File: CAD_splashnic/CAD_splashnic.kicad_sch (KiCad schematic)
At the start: 3 parts, among them J1 Screw_Terminal_01x03, U1 STM32G431KBTx

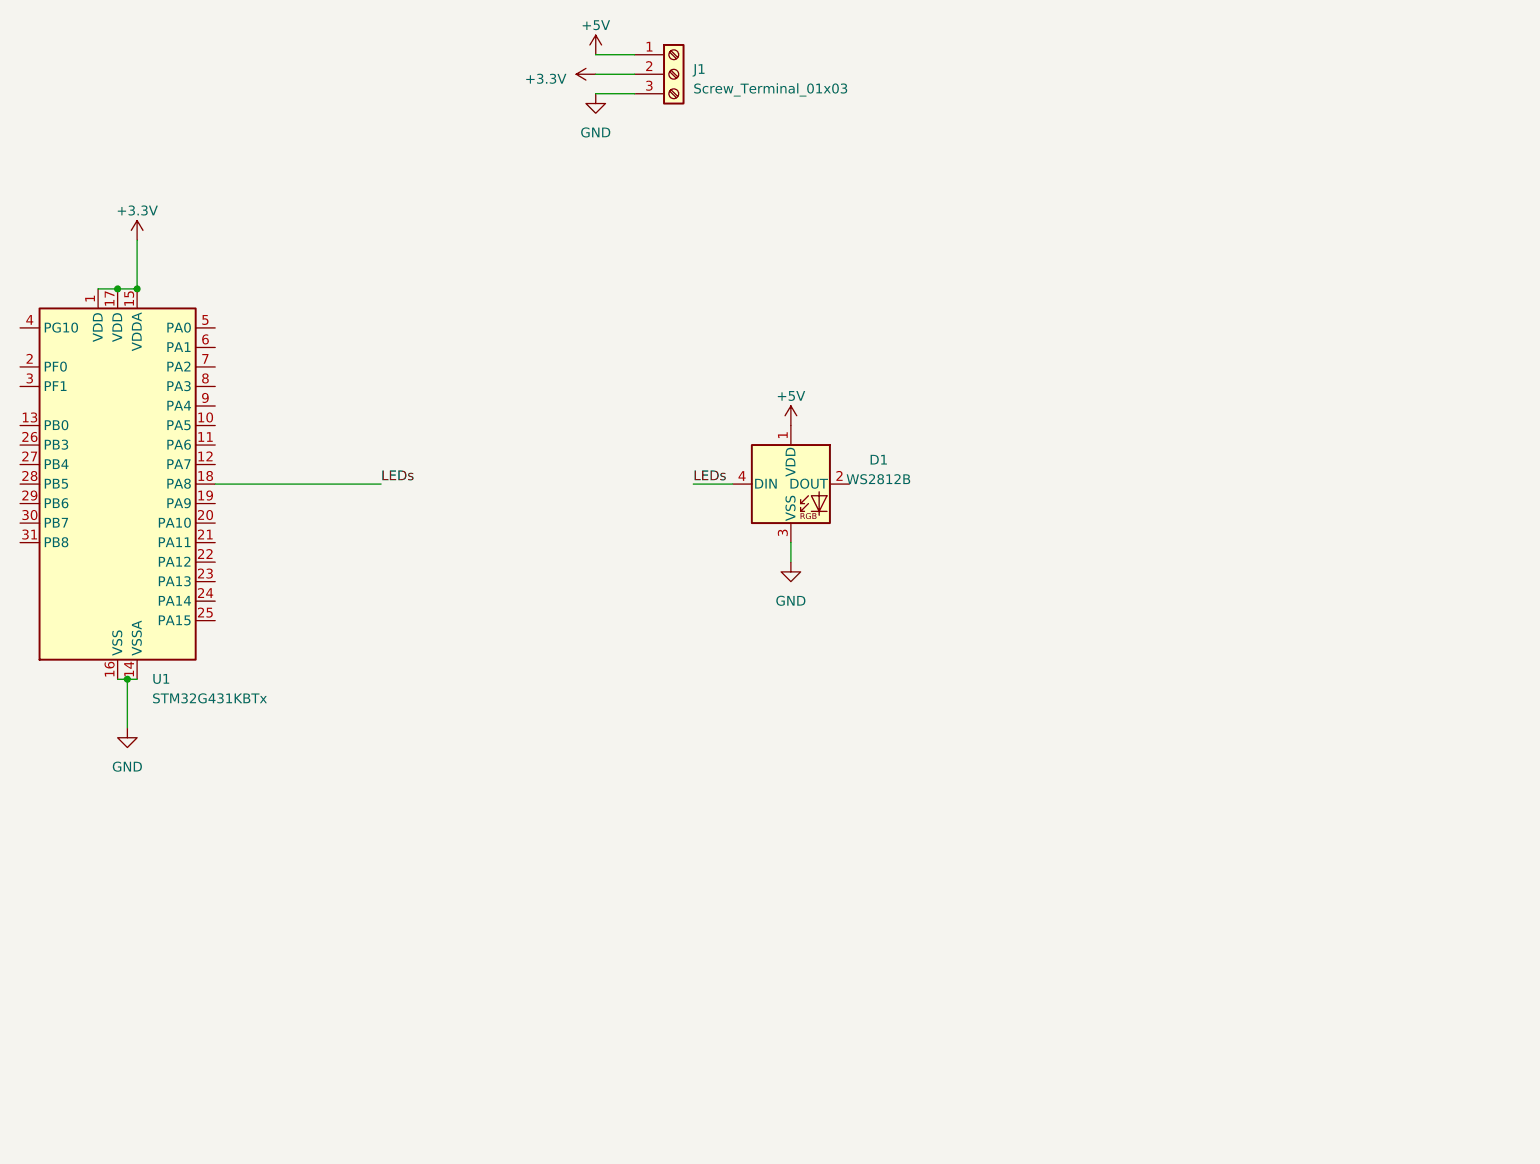
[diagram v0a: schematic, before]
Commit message: integrated GPS to schematics
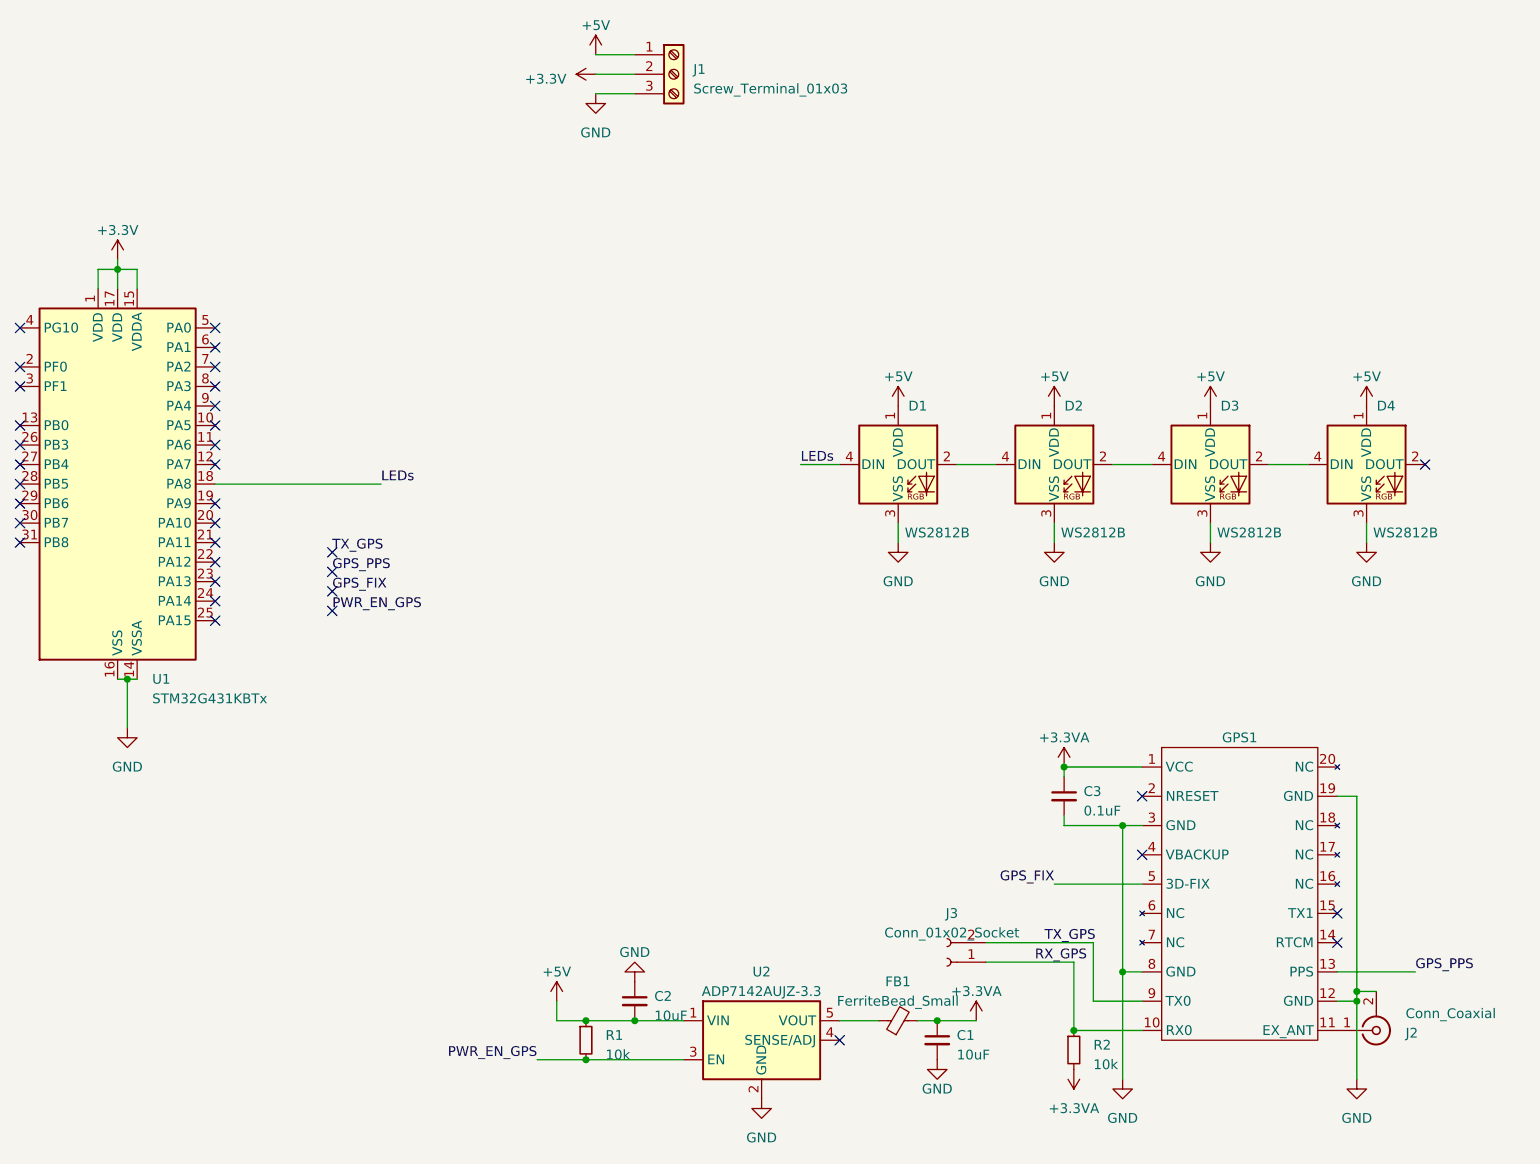
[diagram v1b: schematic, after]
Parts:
- added C1, C2: 10uF, symbol Device:C_Small
- added C3: 0.1uF, symbol Device:C_Small
- added D2, D3, D4: WS2812B, LED_SMD:LED_WS2812B_PLCC4_5.0x5.0mm_P3.2mm, symbol LED:WS2812B
- added FB1: FerriteBead_Small, symbol Device:FerriteBead_Small
- added GPS1: ~, symbol New_Library:PA1616S
- added J2: Conn_Coaxial, symbol Connector:Conn_Coaxial
- added J3: Conn_01x02_Socket, symbol Connector:Conn_01x02_Socket
- added R1, R2: 10k, symbol Device:R_Small
- added U2: ADP7142AUJZ-3.3, Package_TO_SOT_SMD:TSOT-23-5, symbol Regulator_Linear:ADP7142AUJZ-3.3
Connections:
- net +5V: now also C2.2, D2.1 (VDD), D3.1 (VDD), D4.1 (VDD), R1.1, U2.1 (VIN)
- net GND: now also C1.2, C2.1, C3.2, D2.3 (VSS), D3.3 (VSS), D4.3 (VSS), GPS1.12 (GND), GPS1.19 (GND), GPS1.3 (GND), GPS1.8 (GND), J2.2 (Ext), U2.2 (GND)
- net at D1.2 (DOUT): now also D2.4 (DIN)
- new net: D2.2 (DOUT), D3.4 (DIN)
- new net: FB1.1, U2.5 (VOUT)
- new net: D3.2 (DOUT), D4.4 (DIN)
- new net: GPS1.11 (EX_ANT), J2.1 (In)
- new net +3.3VA: C1.1, C3.1, FB1.2, GPS1.1 (VCC), R2.2
- new net GPS_FIX: GPS1.5 (3D-FIX)
- new net GPS_PPS: GPS1.13 (PPS)
- new net PWR_EN_GPS: R1.2, U2.3 (EN)
- new net RX_GPS: GPS1.10 (RX0), J3.1 (Pin_1), R2.1
- new net TX_GPS: GPS1.9 (TX0), J3.2 (Pin_2)
- no-connect marks 0 -> 35
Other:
- moved on the sheet: D1
